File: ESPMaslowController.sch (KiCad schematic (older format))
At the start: 41 parts, among them J1 Barrel_Jack_Switch, J10 Conn_01x03, J11 Conn_01x03, J2 B6B-PH-K-S, J3 B6B-PH-K-S, J4 B6B-PH-K-S, J5 B6B-PH-K-S, J6 B6B-PH-K-S, J7 Micro_SD_Card_Det, J8 Conn_01x03, J9 Conn_02x12_Odd_Even, U1 NCP3063, U2 ESP32-DevKit-Doit, U3 ATmega328PB-AU

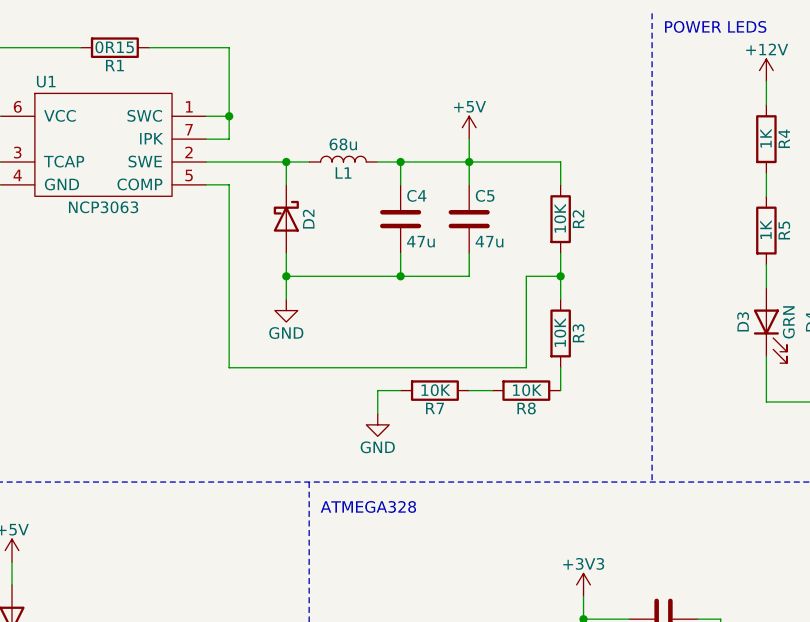
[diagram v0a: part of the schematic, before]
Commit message: Fixed board errors.
Corrected motor connectors to be JST XH series (2.5 mm pitch).
Corrected NCP3063 feedback resistor divider for 5V output.
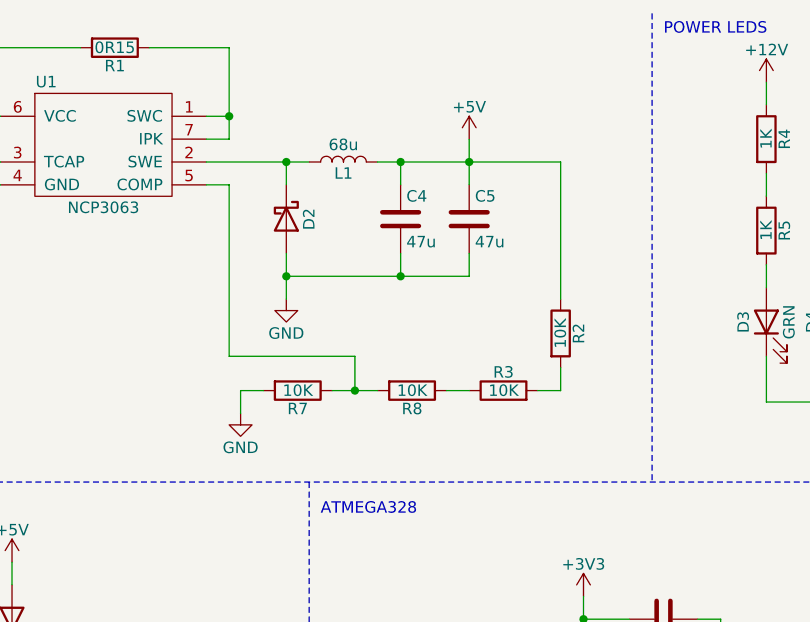
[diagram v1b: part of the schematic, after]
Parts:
- J2, J3, J4, J5, J6: value B6B-PH-K-S -> B6B-XH-A; footprint Connector_JST:JST_PH_B6B-PH-K_1x06_P2.00mm_Vertical -> Connector_JST:JST_XH_B6B-XH-A_1x06_P2.50mm_Vertical
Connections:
- net at R3.2: now also R2.2; no longer R8.1
- net at R7.1, R8.2: now also U1.5 (COMP)
- new net: R3.1, R8.1
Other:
- moved on the sheet: R2, R3, R7, R8
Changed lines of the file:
@@
 L Device:R R?
 U 1 1 5F774D0B
-P 9000 1400
+P 9000 1900
 AR Path="/5F746CB5/5F774D0B" Ref="R?"  Part="1"
 AR Path="/5F774D0B" Ref="R2"  Part="1"
-F 0 "R2" V 9080 1400 50  0000 C CNN
-F 1 "10K" V 9000 1400 50  0000 C CNN
-F 2 "Resistor_SMD:R_0805_2012Metric" V 8930 1400 50  0001 C CNN
-F 3 "https://www.yageo.com/upload/media/product/productsearch/datasheet/rchip/PYu-RC_Group_51_RoHS_L_11.pdf" H 9000 1400 50  0001 C CNN
-F 4 "Yageo" H 9000 1400 50  0001 C CNN "MFR"
-F 5 "RC0805FR-0710KL" H 9000 1400 50  0001 C CNN "MPN"
-F 6 "0.10" H 9000 1400 50  0001 C CNN "Price"
-F 7 "C17414" H 9000 1400 50  0001 C CNN "LCSC"
-	1    9000 1400
+F 0 "R2" V 9080 1900 50  0000 C CNN
+F 1 "10K" V 9000 1900 50  0000 C CNN
+F 2 "Resistor_SMD:R_0805_2012Metric" V 8930 1900 50  0001 C CNN
+F 3 "https://www.yageo.com/upload/media/product/productsearch/datasheet/rchip/PYu-RC_Group_51_RoHS_L_11.pdf" H 9000 1900 50  0001 C CNN
+F 4 "Yageo" H 9000 1900 50  0001 C CNN "MFR"
+F 5 "RC0805FR-0710KL" H 9000 1900 50  0001 C CNN "MPN"
+F 6 "0.10" H 9000 1900 50  0001 C CNN "Price"
+F 7 "C17414" H 9000 1900 50  0001 C CNN "LCSC"
+	1    9000 1900
 	1    0    0    -1
 $EndComp
@@
 Connection ~ 7550 950
 Wire Wire Line
-	9000 1550 9000 1650
-Wire Wire Line
-	9000 1650 8850 1650
-Wire Wire Line
 	7550 1250 7450 1250
-Connection ~ 9000 1650
-Wire Wire Line
-	9000 1650 9000 1750
 $Comp
 L power:GND #PWR?
 U 1 1 5F774D1F
-P 8200 2250
+P 7600 2250
 AR Path="/5F746CB5/5F774D1F" Ref="#PWR?"  Part="1"
 AR Path="/5F774D1F" Ref="#PWR05"  Part="1"
-F 0 "#PWR05" H 8200 2000 50  0001 C CNN
-F 1 "GND" H 8200 2100 50  0000 C CNN
-F 2 "" H 8200 2250 50  0001 C CNN
-F 3 "" H 8200 2250 50  0001 C CNN
-	1    8200 2250
-	1    0    0    -1
-$EndComp
-Wire Wire Line
-	9000 2050 9000 2150
+F 0 "#PWR05" H 7600 2000 50  0001 C CNN
+F 1 "GND" H 7600 2100 50  0000 C CNN
+F 2 "" H 7600 2250 50  0001 C CNN
+F 3 "" H 7600 2250 50  0001 C CNN
+	1    7600 2250
+	1    0    0    -1
+$EndComp
 $Comp
 L power:GND #PWR?
@@
 	8600 1150 9000 1150
 Wire Wire Line
-	9000 1150 9000 1250
-Wire Wire Line
-	8850 1650 8850 2050
-Wire Wire Line
-	8850 2050 7550 2050
-Wire Wire Line
-	7550 1250 7550 2050
+	9000 1150 9000 1750
+Wire Wire Line
+	7550 1250 7550 2000
 $Comp
 L Device:C C?
@@
 AR Path="/604DC41A/604DEB90" Ref="J?"  Part="1"
 F 0 "J2" H 3450 1350 50  0000 C CNN
-F 1 "B6B-PH-K-S" H 3450 650 50  0001 C CNN
-F 2 "Connector_JST:JST_PH_B6B-PH-K_1x06_P2.00mm_Vertical" H 3450 1050 50  0001 C CNN
+F 1 "B6B-XH-A" H 3450 650 50  0001 C CNN
+F 2 "Connector_JST:JST_XH_B6B-XH-A_1x06_P2.50mm_Vertical" H 3450 1050 50  0001 C CNN
 F 3 "http://www.jst-mfg.com/product/pdf/eng/ePH.pdf" H 3450 1050 50  0001 C CNN
 F 4 "B6B-PH-K-S(LF)(SN)" H 3450 1050 50  0001 C CNN "MPN"
@@
 AR Path="/604DC41A/5FA22EF0" Ref="J?"  Part="1"
 F 0 "J3" H 3450 2550 50  0000 C CNN
-F 1 "B6B-PH-K-S" H 3450 1850 50  0001 C CNN
-F 2 "Connector_JST:JST_PH_B6B-PH-K_1x06_P2.00mm_Vertical" H 3450 2250 50  0001 C CNN
+F 1 "B6B-XH-A" H 3450 1850 50  0001 C CNN
+F 2 "Connector_JST:JST_XH_B6B-XH-A_1x06_P2.50mm_Vertical" H 3450 2250 50  0001 C CNN
 F 3 "http://www.jst-mfg.com/product/pdf/eng/ePH.pdf" H 3450 2250 50  0001 C CNN
 F 4 "B6B-PH-K-S(LF)(SN)" H 3450 2250 50  0001 C CNN "MPN"
@@
 AR Path="/604DC41A/5FA23815" Ref="J?"  Part="1"
 F 0 "J4" H 3450 3750 50  0000 C CNN
-F 1 "B6B-PH-K-S" H 3450 3050 50  0001 C CNN
-F 2 "Connector_JST:JST_PH_B6B-PH-K_1x06_P2.00mm_Vertical" H 3450 3450 50  0001 C CNN
+F 1 "B6B-XH-A" H 3450 3050 50  0001 C CNN
+F 2 "Connector_JST:JST_XH_B6B-XH-A_1x06_P2.50mm_Vertical" H 3450 3450 50  0001 C CNN
 F 3 "http://www.jst-mfg.com/product/pdf/eng/ePH.pdf" H 3450 3450 50  0001 C CNN
 F 4 "B6B-PH-K-S(LF)(SN)" H 3450 3450 50  0001 C CNN "MPN"
@@
 AR Path="/604DC41A/5FA3EE82" Ref="J?"  Part="1"
 F 0 "J5" H 3450 4950 50  0000 C CNN
-F 1 "B6B-PH-K-S" H 3450 4250 50  0001 C CNN
-F 2 "Connector_JST:JST_PH_B6B-PH-K_1x06_P2.00mm_Vertical" H 3450 4650 50  0001 C CNN
+F 1 "B6B-XH-A" H 3450 4250 50  0001 C CNN
+F 2 "Connector_JST:JST_XH_B6B-XH-A_1x06_P2.50mm_Vertical" H 3450 4650 50  0001 C CNN
 F 3 "http://www.jst-mfg.com/product/pdf/eng/ePH.pdf" H 3450 4650 50  0001 C CNN
 F 4 "B6B-PH-K-S(LF)(SN)" H 3450 4650 50  0001 C CNN "MPN"
@@
 AR Path="/604DC41A/5FA4CC02" Ref="J?"  Part="1"
 F 0 "J6" H 3450 6150 50  0000 C CNN
-F 1 "B6B-PH-K-S" H 3450 5450 50  0001 C CNN
-F 2 "Connector_JST:JST_PH_B6B-PH-K_1x06_P2.00mm_Vertical" H 3450 5850 50  0001 C CNN
+F 1 "B6B-XH-A" H 3450 5450 50  0001 C CNN
+F 2 "Connector_JST:JST_XH_B6B-XH-A_1x06_P2.50mm_Vertical" H 3450 5850 50  0001 C CNN
 F 3 "http://www.jst-mfg.com/product/pdf/eng/ePH.pdf" H 3450 5850 50  0001 C CNN
 F 4 "B6B-PH-K-S(LF)(SN)" H 3450 5850 50  0001 C CNN "MPN"
@@
 L Device:R R?
 U 1 1 5F7BF536
-P 9000 1900
+P 8750 2150
 AR Path="/5F746CB5/5F7BF536" Ref="R?"  Part="1"
 AR Path="/5F7BF536" Ref="R3"  Part="1"
-F 0 "R3" V 9080 1900 50  0000 C CNN
-F 1 "10K" V 9000 1900 50  0000 C CNN
-F 2 "Resistor_SMD:R_0805_2012Metric" V 8930 1900 50  0001 C CNN
-F 3 "https://www.yageo.com/upload/media/product/productsearch/datasheet/rchip/PYu-RC_Group_51_RoHS_L_11.pdf" H 9000 1900 50  0001 C CNN
-F 4 "Yageo" H 9000 1900 50  0001 C CNN "MFR"
-F 5 "RC0805FR-0710KL" H 9000 1900 50  0001 C CNN "MPN"
-F 6 "0.10" H 9000 1900 50  0001 C CNN "Price"
-F 7 "C17414" H 9000 1900 50  0001 C CNN "LCSC"
-	1    9000 1900
-	1    0    0    -1
+F 0 "R3" V 8830 2150 50  0000 C CNN
+F 1 "10K" V 8750 2150 50  0000 C CNN
+F 2 "Resistor_SMD:R_0805_2012Metric" V 8680 2150 50  0001 C CNN
+F 3 "https://www.yageo.com/upload/media/product/productsearch/datasheet/rchip/PYu-RC_Group_51_RoHS_L_11.pdf" H 8750 2150 50  0001 C CNN
+F 4 "Yageo" H 8750 2150 50  0001 C CNN "MFR"
+F 5 "RC0805FR-0710KL" H 8750 2150 50  0001 C CNN "MPN"
+F 6 "0.10" H 8750 2150 50  0001 C CNN "Price"
+F 7 "C17414" H 8750 2150 50  0001 C CNN "LCSC"
+	1    8750 2150
+	0    -1   -1   0
 $EndComp
 $Comp
 L Device:R R?
 U 1 1 5F7BFB17
-P 8850 2150
+P 8350 2150
 AR Path="/5F746CB5/5F7BFB17" Ref="R?"  Part="1"
 AR Path="/5F7BFB17" Ref="R8"  Part="1"
-F 0 "R8" V 8930 2150 50  0000 C CNN
-F 1 "10K" V 8850 2150 50  0000 C CNN
-F 2 "Resistor_SMD:R_0805_2012Metric" V 8780 2150 50  0001 C CNN
-F 3 "https://www.yageo.com/upload/media/product/productsearch/datasheet/rchip/PYu-RC_Group_51_RoHS_L_11.pdf" H 8850 2150 50  0001 C CNN
-F 4 "Yageo" H 8850 2150 50  0001 C CNN "MFR"
-F 5 "RC0805FR-0710KL" H 8850 2150 50  0001 C CNN "MPN"
-F 6 "0.10" H 8850 2150 50  0001 C CNN "Price"
-F 7 "C17414" H 8850 2150 50  0001 C CNN "LCSC"
-	1    8850 2150
+F 0 "R8" V 8430 2150 50  0000 C CNN
+F 1 "10K" V 8350 2150 50  0000 C CNN
+F 2 "Resistor_SMD:R_0805_2012Metric" V 8280 2150 50  0001 C CNN
+F 3 "https://www.yageo.com/upload/media/product/productsearch/datasheet/rchip/PYu-RC_Group_51_RoHS_L_11.pdf" H 8350 2150 50  0001 C CNN
+F 4 "Yageo" H 8350 2150 50  0001 C CNN "MFR"
+F 5 "RC0805FR-0710KL" H 8350 2150 50  0001 C CNN "MPN"
+F 6 "0.10" H 8350 2150 50  0001 C CNN "Price"
+F 7 "C17414" H 8350 2150 50  0001 C CNN "LCSC"
+	1    8350 2150
 	0    1    1    0
 $EndComp
@@
 L Device:R R?
 U 1 1 5F7C00C8
-P 8450 2150
+P 7850 2150
 AR Path="/5F746CB5/5F7C00C8" Ref="R?"  Part="1"
 AR Path="/5F7C00C8" Ref="R7"  Part="1"
-F 0 "R7" V 8530 2150 50  0000 C CNN
-F 1 "10K" V 8450 2150 50  0000 C CNN
-F 2 "Resistor_SMD:R_0805_2012Metric" V 8380 2150 50  0001 C CNN
-F 3 "https://www.yageo.com/upload/media/product/productsearch/datasheet/rchip/PYu-RC_Group_51_RoHS_L_11.pdf" H 8450 2150 50  0001 C CNN
-F 4 "Yageo" H 8450 2150 50  0001 C CNN "MFR"
-F 5 "RC0805FR-0710KL" H 8450 2150 50  0001 C CNN "MPN"
-F 6 "0.10" H 8450 2150 50  0001 C CNN "Price"
-F 7 "C17414" H 8450 2150 50  0001 C CNN "LCSC"
-	1    8450 2150
+F 0 "R7" V 7930 2150 50  0000 C CNN
+F 1 "10K" V 7850 2150 50  0000 C CNN
+F 2 "Resistor_SMD:R_0805_2012Metric" V 7780 2150 50  0001 C CNN
+F 3 "https://www.yageo.com/upload/media/product/productsearch/datasheet/rchip/PYu-RC_Group_51_RoHS_L_11.pdf" H 7850 2150 50  0001 C CNN
+F 4 "Yageo" H 7850 2150 50  0001 C CNN "MFR"
+F 5 "RC0805FR-0710KL" H 7850 2150 50  0001 C CNN "MPN"
+F 6 "0.10" H 7850 2150 50  0001 C CNN "Price"
+F 7 "C17414" H 7850 2150 50  0001 C CNN "LCSC"
+	1    7850 2150
 	0    1    1    0
 $EndComp
 Wire Wire Line
-	8600 2150 8700 2150
-Wire Wire Line
-	8300 2150 8200 2150
-Wire Wire Line
-	8200 2150 8200 2250
+	8000 2150 8100 2150
+Wire Wire Line
+	7700 2150 7600 2150
+Wire Wire Line
+	7600 2150 7600 2250
 Text Label 2100 7750 0    50   ~ 0
 PWM6
@@
 Wire Wire Line
 	5750 5750 5250 5750
+Wire Wire Line
+	8500 2150 8600 2150
+Wire Wire Line
+	7550 2000 8100 2000
+Wire Wire Line
+	8100 2000 8100 2150
+Connection ~ 8100 2150
+Wire Wire Line
+	8100 2150 8200 2150
+Wire Wire Line
+	8900 2150 9000 2150
+Wire Wire Line
+	9000 2150 9000 2050
 $EndSCHEMATC
